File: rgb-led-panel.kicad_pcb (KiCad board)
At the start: 2 copper layers, 26 parts

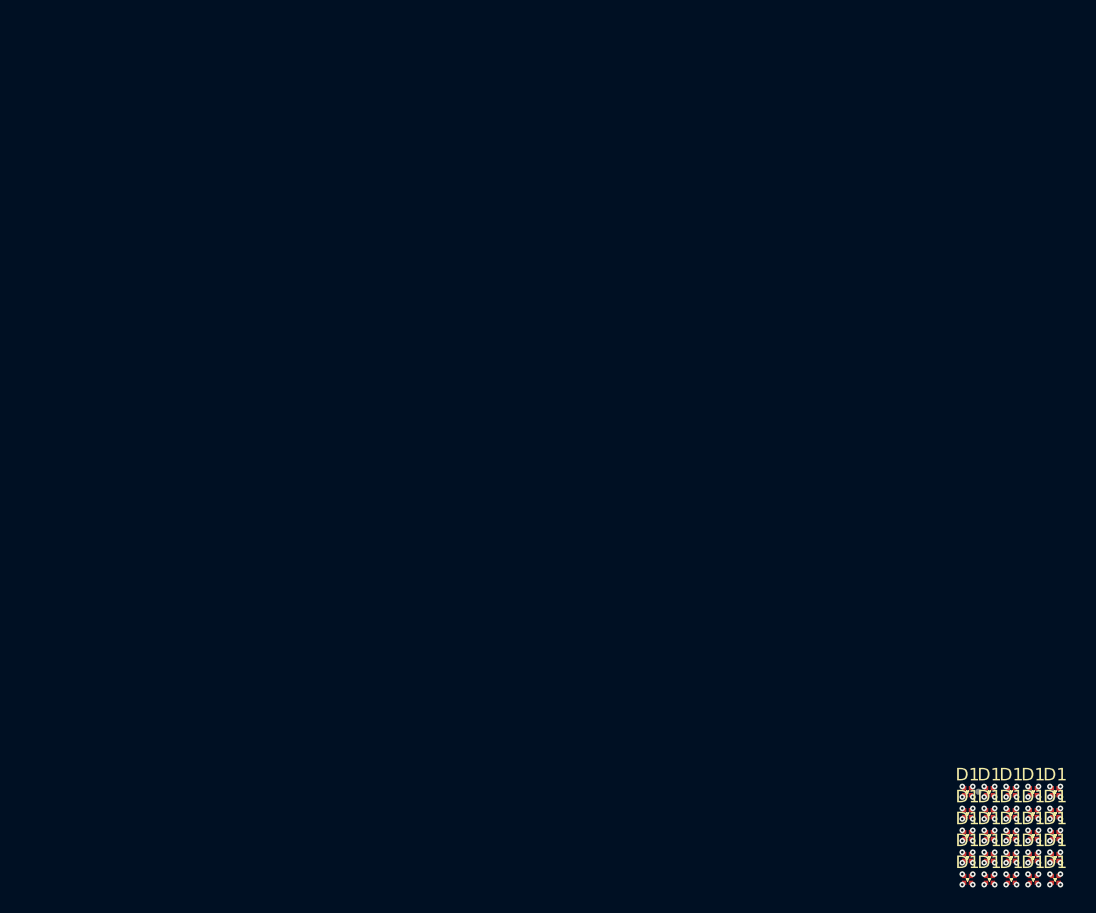
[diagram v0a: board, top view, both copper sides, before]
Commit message: Layout 16x16 RGB panel
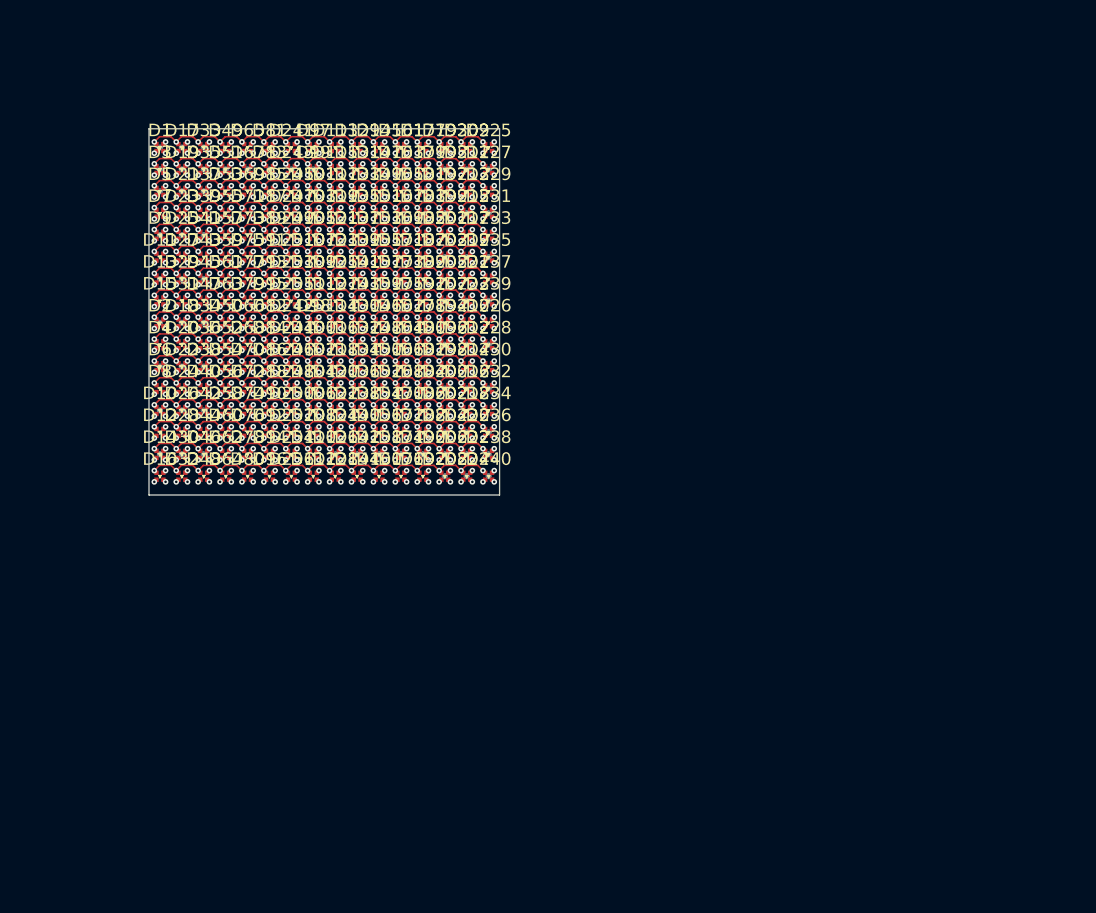
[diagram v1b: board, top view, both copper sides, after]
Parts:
- removed the D1 at (121.5, 108.5)
- removed the D1 at (114.5, 106.7)
- removed the D1 at (121.5, 105.0)
- removed the D1 at (119.8, 105.0)
- removed the D1 at (118.0, 105.0)
- removed the D1 at (116.2, 105.0)
- removed the D1 at (114.5, 105.0)
- removed the D1 at (121.5, 103.2)
- removed the D1 at (119.8, 103.2)
- removed the D1 at (118.0, 103.2)
- removed the D1 at (116.2, 103.2)
- removed the D1 at (119.8, 108.5)
- removed the D1 at (114.5, 103.2)
- removed the D1 at (121.5, 101.5)
- removed the D1 at (119.8, 101.5)
- removed the D1 at (118.0, 101.5)
- removed the D1 at (116.2, 101.5)
- removed the D1 at (114.5, 101.5)
- removed the D1 at (118.0, 108.5)
- removed the D1 at (116.2, 108.5)
- removed the D1 at (114.5, 108.5)
- removed the D1 at (121.5, 106.7)
- removed the D1 at (119.8, 106.7)
- removed the D1 at (118.0, 106.7)
- removed the D1 at (116.2, 106.7)
- removed REF**: TestPoint_0.5mm, TestPoint_Small:TestPoint_0.5mm
- added D1: LED_ARGB, LED_SMD_RGB:MHPA0808RGBDT, F.Cu at (50.0, 50.0)
- added D10: LED_ARGB, LED_SMD_RGB:MHPA0808RGBDT, F.Cu at (50.0, 71.0)
- added D100: LED_ARGB, LED_SMD_RGB:MHPA0808RGBDT, F.Cu at (62.2, 65.8)
- added D101: LED_ARGB, LED_SMD_RGB:MHPA0808RGBDT, F.Cu at (62.2, 53.5)
- added D102: LED_ARGB, LED_SMD_RGB:MHPA0808RGBDT, F.Cu at (62.2, 67.5)
- added D103: LED_ARGB, LED_SMD_RGB:MHPA0808RGBDT, F.Cu at (62.2, 55.2)
- added D104: LED_ARGB, LED_SMD_RGB:MHPA0808RGBDT, F.Cu at (62.2, 69.2)
- added D105: LED_ARGB, LED_SMD_RGB:MHPA0808RGBDT, F.Cu at (62.2, 57.0)
- added D106: LED_ARGB, LED_SMD_RGB:MHPA0808RGBDT, F.Cu at (62.2, 71.0)
- added D107: LED_ARGB, LED_SMD_RGB:MHPA0808RGBDT, F.Cu at (62.2, 58.8)
- added D108: LED_ARGB, LED_SMD_RGB:MHPA0808RGBDT, F.Cu at (62.2, 72.8)
- added D109: LED_ARGB, LED_SMD_RGB:MHPA0808RGBDT, F.Cu at (62.2, 60.5)
- added D11: LED_ARGB, LED_SMD_RGB:MHPA0808RGBDT, F.Cu at (50.0, 58.8)
- added D110: LED_ARGB, LED_SMD_RGB:MHPA0808RGBDT, F.Cu at (62.2, 74.5)
- added D111: LED_ARGB, LED_SMD_RGB:MHPA0808RGBDT, F.Cu at (62.2, 62.2)
- added D112: LED_ARGB, LED_SMD_RGB:MHPA0808RGBDT, F.Cu at (62.2, 76.2)
- added D113: LED_ARGB, LED_SMD_RGB:MHPA0808RGBDT, F.Cu at (64.0, 50.0)
- added D114: LED_ARGB, LED_SMD_RGB:MHPA0808RGBDT, F.Cu at (64.0, 64.0)
- added D115: LED_ARGB, LED_SMD_RGB:MHPA0808RGBDT, F.Cu at (64.0, 51.8)
- added D116: LED_ARGB, LED_SMD_RGB:MHPA0808RGBDT, F.Cu at (64.0, 65.8)
- added D117: LED_ARGB, LED_SMD_RGB:MHPA0808RGBDT, F.Cu at (64.0, 53.5)
- added D118: LED_ARGB, LED_SMD_RGB:MHPA0808RGBDT, F.Cu at (64.0, 67.5)
- added D119: LED_ARGB, LED_SMD_RGB:MHPA0808RGBDT, F.Cu at (64.0, 55.2)
- added D12: LED_ARGB, LED_SMD_RGB:MHPA0808RGBDT, F.Cu at (50.0, 72.8)
- added D120: LED_ARGB, LED_SMD_RGB:MHPA0808RGBDT, F.Cu at (64.0, 69.2)
- added D121: LED_ARGB, LED_SMD_RGB:MHPA0808RGBDT, F.Cu at (64.0, 57.0)
- added D122: LED_ARGB, LED_SMD_RGB:MHPA0808RGBDT, F.Cu at (64.0, 71.0)
- added D123: LED_ARGB, LED_SMD_RGB:MHPA0808RGBDT, F.Cu at (64.0, 58.8)
- added D124: LED_ARGB, LED_SMD_RGB:MHPA0808RGBDT, F.Cu at (64.0, 72.8)
- added D125: LED_ARGB, LED_SMD_RGB:MHPA0808RGBDT, F.Cu at (64.0, 60.5)
- added D126: LED_ARGB, LED_SMD_RGB:MHPA0808RGBDT, F.Cu at (64.0, 74.5)
- added D127: LED_ARGB, LED_SMD_RGB:MHPA0808RGBDT, F.Cu at (64.0, 62.2)
- added D128: LED_ARGB, LED_SMD_RGB:MHPA0808RGBDT, F.Cu at (64.0, 76.2)
- added D129: LED_ARGB, LED_SMD_RGB:MHPA0808RGBDT, F.Cu at (65.8, 50.0)
- added D13: LED_ARGB, LED_SMD_RGB:MHPA0808RGBDT, F.Cu at (50.0, 60.5)
- added D130: LED_ARGB, LED_SMD_RGB:MHPA0808RGBDT, F.Cu at (65.8, 64.0)
- added D131: LED_ARGB, LED_SMD_RGB:MHPA0808RGBDT, F.Cu at (65.8, 51.8)
- added D132: LED_ARGB, LED_SMD_RGB:MHPA0808RGBDT, F.Cu at (65.8, 65.8)
- added D133: LED_ARGB, LED_SMD_RGB:MHPA0808RGBDT, F.Cu at (65.8, 53.5)
- added D134: LED_ARGB, LED_SMD_RGB:MHPA0808RGBDT, F.Cu at (65.8, 67.5)
- added D135: LED_ARGB, LED_SMD_RGB:MHPA0808RGBDT, F.Cu at (65.8, 55.2)
- added D136: LED_ARGB, LED_SMD_RGB:MHPA0808RGBDT, F.Cu at (65.8, 69.2)
- added D137: LED_ARGB, LED_SMD_RGB:MHPA0808RGBDT, F.Cu at (65.8, 57.0)
- added D138: LED_ARGB, LED_SMD_RGB:MHPA0808RGBDT, F.Cu at (65.8, 71.0)
- added D139: LED_ARGB, LED_SMD_RGB:MHPA0808RGBDT, F.Cu at (65.8, 58.8)
- added D14: LED_ARGB, LED_SMD_RGB:MHPA0808RGBDT, F.Cu at (50.0, 74.5)
- added D140: LED_ARGB, LED_SMD_RGB:MHPA0808RGBDT, F.Cu at (65.8, 72.8)
- added D141: LED_ARGB, LED_SMD_RGB:MHPA0808RGBDT, F.Cu at (65.8, 60.5)
- added D142: LED_ARGB, LED_SMD_RGB:MHPA0808RGBDT, F.Cu at (65.8, 74.5)
- added D143: LED_ARGB, LED_SMD_RGB:MHPA0808RGBDT, F.Cu at (65.8, 62.2)
- added D144: LED_ARGB, LED_SMD_RGB:MHPA0808RGBDT, F.Cu at (65.8, 76.2)
- added D145: LED_ARGB, LED_SMD_RGB:MHPA0808RGBDT, F.Cu at (67.5, 50.0)
- added D146: LED_ARGB, LED_SMD_RGB:MHPA0808RGBDT, F.Cu at (67.5, 64.0)
- added D147: LED_ARGB, LED_SMD_RGB:MHPA0808RGBDT, F.Cu at (67.5, 51.8)
- added D148: LED_ARGB, LED_SMD_RGB:MHPA0808RGBDT, F.Cu at (67.5, 65.8)
- added D149: LED_ARGB, LED_SMD_RGB:MHPA0808RGBDT, F.Cu at (67.5, 53.5)
- added D15: LED_ARGB, LED_SMD_RGB:MHPA0808RGBDT, F.Cu at (50.0, 62.2)
- added D150: LED_ARGB, LED_SMD_RGB:MHPA0808RGBDT, F.Cu at (67.5, 67.5)
- added D151: LED_ARGB, LED_SMD_RGB:MHPA0808RGBDT, F.Cu at (67.5, 55.2)
- added D152: LED_ARGB, LED_SMD_RGB:MHPA0808RGBDT, F.Cu at (67.5, 69.2)
- added D153: LED_ARGB, LED_SMD_RGB:MHPA0808RGBDT, F.Cu at (67.5, 57.0)
- added D154: LED_ARGB, LED_SMD_RGB:MHPA0808RGBDT, F.Cu at (67.5, 71.0)
- added D155: LED_ARGB, LED_SMD_RGB:MHPA0808RGBDT, F.Cu at (67.5, 58.8)
- added D156: LED_ARGB, LED_SMD_RGB:MHPA0808RGBDT, F.Cu at (67.5, 72.8)
- added D157: LED_ARGB, LED_SMD_RGB:MHPA0808RGBDT, F.Cu at (67.5, 60.5)
- added D158: LED_ARGB, LED_SMD_RGB:MHPA0808RGBDT, F.Cu at (67.5, 74.5)
- added D159: LED_ARGB, LED_SMD_RGB:MHPA0808RGBDT, F.Cu at (67.5, 62.2)
- added D16: LED_ARGB, LED_SMD_RGB:MHPA0808RGBDT, F.Cu at (50.0, 76.2)
- added D160: LED_ARGB, LED_SMD_RGB:MHPA0808RGBDT, F.Cu at (67.5, 76.2)
- added D161: LED_ARGB, LED_SMD_RGB:MHPA0808RGBDT, F.Cu at (69.2, 50.0)
- added D162: LED_ARGB, LED_SMD_RGB:MHPA0808RGBDT, F.Cu at (69.2, 64.0)
- added D163: LED_ARGB, LED_SMD_RGB:MHPA0808RGBDT, F.Cu at (69.2, 51.8)
- added D164: LED_ARGB, LED_SMD_RGB:MHPA0808RGBDT, F.Cu at (69.2, 65.8)
- added D165: LED_ARGB, LED_SMD_RGB:MHPA0808RGBDT, F.Cu at (69.2, 53.5)
- added D166: LED_ARGB, LED_SMD_RGB:MHPA0808RGBDT, F.Cu at (69.2, 67.5)
- added D167: LED_ARGB, LED_SMD_RGB:MHPA0808RGBDT, F.Cu at (69.2, 55.2)
- added D168: LED_ARGB, LED_SMD_RGB:MHPA0808RGBDT, F.Cu at (69.2, 69.2)
- added D169: LED_ARGB, LED_SMD_RGB:MHPA0808RGBDT, F.Cu at (69.2, 57.0)
- added D17: LED_ARGB, LED_SMD_RGB:MHPA0808RGBDT, F.Cu at (51.8, 50.0)
- added D170: LED_ARGB, LED_SMD_RGB:MHPA0808RGBDT, F.Cu at (69.2, 71.0)
- added D171: LED_ARGB, LED_SMD_RGB:MHPA0808RGBDT, F.Cu at (69.2, 58.8)
- added D172: LED_ARGB, LED_SMD_RGB:MHPA0808RGBDT, F.Cu at (69.2, 72.8)
- added D173: LED_ARGB, LED_SMD_RGB:MHPA0808RGBDT, F.Cu at (69.2, 60.5)
- added D174: LED_ARGB, LED_SMD_RGB:MHPA0808RGBDT, F.Cu at (69.2, 74.5)
- added D175: LED_ARGB, LED_SMD_RGB:MHPA0808RGBDT, F.Cu at (69.2, 62.2)
- added D176: LED_ARGB, LED_SMD_RGB:MHPA0808RGBDT, F.Cu at (69.2, 76.2)
- added D177: LED_ARGB, LED_SMD_RGB:MHPA0808RGBDT, F.Cu at (71.0, 50.0)
- added D178: LED_ARGB, LED_SMD_RGB:MHPA0808RGBDT, F.Cu at (71.0, 64.0)
- added D179: LED_ARGB, LED_SMD_RGB:MHPA0808RGBDT, F.Cu at (71.0, 51.8)
- added D18: LED_ARGB, LED_SMD_RGB:MHPA0808RGBDT, F.Cu at (51.8, 64.0)
- added D180: LED_ARGB, LED_SMD_RGB:MHPA0808RGBDT, F.Cu at (71.0, 65.8)
- added D181: LED_ARGB, LED_SMD_RGB:MHPA0808RGBDT, F.Cu at (71.0, 53.5)
- added D182: LED_ARGB, LED_SMD_RGB:MHPA0808RGBDT, F.Cu at (71.0, 67.5)
- added D183: LED_ARGB, LED_SMD_RGB:MHPA0808RGBDT, F.Cu at (71.0, 55.2)
- added D184: LED_ARGB, LED_SMD_RGB:MHPA0808RGBDT, F.Cu at (71.0, 69.2)
- added D185: LED_ARGB, LED_SMD_RGB:MHPA0808RGBDT, F.Cu at (71.0, 57.0)
- added D186: LED_ARGB, LED_SMD_RGB:MHPA0808RGBDT, F.Cu at (71.0, 71.0)
- added D187: LED_ARGB, LED_SMD_RGB:MHPA0808RGBDT, F.Cu at (71.0, 58.8)
- added D188: LED_ARGB, LED_SMD_RGB:MHPA0808RGBDT, F.Cu at (71.0, 72.8)
- added D189: LED_ARGB, LED_SMD_RGB:MHPA0808RGBDT, F.Cu at (71.0, 60.5)
- added D19: LED_ARGB, LED_SMD_RGB:MHPA0808RGBDT, F.Cu at (51.8, 51.8)
- added D190: LED_ARGB, LED_SMD_RGB:MHPA0808RGBDT, F.Cu at (71.0, 74.5)
- added D191: LED_ARGB, LED_SMD_RGB:MHPA0808RGBDT, F.Cu at (71.0, 62.2)
- added D192: LED_ARGB, LED_SMD_RGB:MHPA0808RGBDT, F.Cu at (71.0, 76.2)
- added D193: LED_ARGB, LED_SMD_RGB:MHPA0808RGBDT, F.Cu at (72.8, 50.0)
- added D194: LED_ARGB, LED_SMD_RGB:MHPA0808RGBDT, F.Cu at (72.8, 64.0)
- added D195: LED_ARGB, LED_SMD_RGB:MHPA0808RGBDT, F.Cu at (72.8, 51.8)
- added D196: LED_ARGB, LED_SMD_RGB:MHPA0808RGBDT, F.Cu at (72.8, 65.8)
- added D197: LED_ARGB, LED_SMD_RGB:MHPA0808RGBDT, F.Cu at (72.8, 53.5)
- added D198: LED_ARGB, LED_SMD_RGB:MHPA0808RGBDT, F.Cu at (72.8, 67.5)
- added D199: LED_ARGB, LED_SMD_RGB:MHPA0808RGBDT, F.Cu at (72.8, 55.2)
- added D2: LED_ARGB, LED_SMD_RGB:MHPA0808RGBDT, F.Cu at (50.0, 64.0)
- added D20: LED_ARGB, LED_SMD_RGB:MHPA0808RGBDT, F.Cu at (51.8, 65.8)
- added D200: LED_ARGB, LED_SMD_RGB:MHPA0808RGBDT, F.Cu at (72.8, 69.2)
- added D201: LED_ARGB, LED_SMD_RGB:MHPA0808RGBDT, F.Cu at (72.8, 57.0)
- added D202: LED_ARGB, LED_SMD_RGB:MHPA0808RGBDT, F.Cu at (72.8, 71.0)
- added D203: LED_ARGB, LED_SMD_RGB:MHPA0808RGBDT, F.Cu at (72.8, 58.8)
- added D204: LED_ARGB, LED_SMD_RGB:MHPA0808RGBDT, F.Cu at (72.8, 72.8)
- added D205: LED_ARGB, LED_SMD_RGB:MHPA0808RGBDT, F.Cu at (72.8, 60.5)
- added D206: LED_ARGB, LED_SMD_RGB:MHPA0808RGBDT, F.Cu at (72.8, 74.5)
- added D207: LED_ARGB, LED_SMD_RGB:MHPA0808RGBDT, F.Cu at (72.8, 62.2)
- added D208: LED_ARGB, LED_SMD_RGB:MHPA0808RGBDT, F.Cu at (72.8, 76.2)
- added D209: LED_ARGB, LED_SMD_RGB:MHPA0808RGBDT, F.Cu at (74.5, 50.0)
- added D21: LED_ARGB, LED_SMD_RGB:MHPA0808RGBDT, F.Cu at (51.8, 53.5)
- added D210: LED_ARGB, LED_SMD_RGB:MHPA0808RGBDT, F.Cu at (74.5, 64.0)
- added D211: LED_ARGB, LED_SMD_RGB:MHPA0808RGBDT, F.Cu at (74.5, 51.8)
- added D212: LED_ARGB, LED_SMD_RGB:MHPA0808RGBDT, F.Cu at (74.5, 65.8)
- added D213: LED_ARGB, LED_SMD_RGB:MHPA0808RGBDT, F.Cu at (74.5, 53.5)
- added D214: LED_ARGB, LED_SMD_RGB:MHPA0808RGBDT, F.Cu at (74.5, 67.5)
- added D215: LED_ARGB, LED_SMD_RGB:MHPA0808RGBDT, F.Cu at (74.5, 55.2)
- added D216: LED_ARGB, LED_SMD_RGB:MHPA0808RGBDT, F.Cu at (74.5, 69.2)
- added D217: LED_ARGB, LED_SMD_RGB:MHPA0808RGBDT, F.Cu at (74.5, 57.0)
- added D218: LED_ARGB, LED_SMD_RGB:MHPA0808RGBDT, F.Cu at (74.5, 71.0)
- added D219: LED_ARGB, LED_SMD_RGB:MHPA0808RGBDT, F.Cu at (74.5, 58.8)
- added D22: LED_ARGB, LED_SMD_RGB:MHPA0808RGBDT, F.Cu at (51.8, 67.5)
- added D220: LED_ARGB, LED_SMD_RGB:MHPA0808RGBDT, F.Cu at (74.5, 72.8)
- added D221: LED_ARGB, LED_SMD_RGB:MHPA0808RGBDT, F.Cu at (74.5, 60.5)
- added D222: LED_ARGB, LED_SMD_RGB:MHPA0808RGBDT, F.Cu at (74.5, 74.5)
- added D223: LED_ARGB, LED_SMD_RGB:MHPA0808RGBDT, F.Cu at (74.5, 62.2)
- added D224: LED_ARGB, LED_SMD_RGB:MHPA0808RGBDT, F.Cu at (74.5, 76.2)
- added D225: LED_ARGB, LED_SMD_RGB:MHPA0808RGBDT, F.Cu at (76.2, 50.0)
- added D226: LED_ARGB, LED_SMD_RGB:MHPA0808RGBDT, F.Cu at (76.2, 64.0)
- added D227: LED_ARGB, LED_SMD_RGB:MHPA0808RGBDT, F.Cu at (76.2, 51.8)
- added D228: LED_ARGB, LED_SMD_RGB:MHPA0808RGBDT, F.Cu at (76.2, 65.8)
- added D229: LED_ARGB, LED_SMD_RGB:MHPA0808RGBDT, F.Cu at (76.2, 53.5)
- added D23: LED_ARGB, LED_SMD_RGB:MHPA0808RGBDT, F.Cu at (51.8, 55.2)
- added D230: LED_ARGB, LED_SMD_RGB:MHPA0808RGBDT, F.Cu at (76.2, 67.5)
- added D231: LED_ARGB, LED_SMD_RGB:MHPA0808RGBDT, F.Cu at (76.2, 55.2)
- added D232: LED_ARGB, LED_SMD_RGB:MHPA0808RGBDT, F.Cu at (76.2, 69.2)
- added D233: LED_ARGB, LED_SMD_RGB:MHPA0808RGBDT, F.Cu at (76.2, 57.0)
- added D234: LED_ARGB, LED_SMD_RGB:MHPA0808RGBDT, F.Cu at (76.2, 71.0)
- added D235: LED_ARGB, LED_SMD_RGB:MHPA0808RGBDT, F.Cu at (76.2, 58.8)
- added D236: LED_ARGB, LED_SMD_RGB:MHPA0808RGBDT, F.Cu at (76.2, 72.8)
- added D237: LED_ARGB, LED_SMD_RGB:MHPA0808RGBDT, F.Cu at (76.2, 60.5)
- added D238: LED_ARGB, LED_SMD_RGB:MHPA0808RGBDT, F.Cu at (76.2, 74.5)
- added D239: LED_ARGB, LED_SMD_RGB:MHPA0808RGBDT, F.Cu at (76.2, 62.2)
- added D24: LED_ARGB, LED_SMD_RGB:MHPA0808RGBDT, F.Cu at (51.8, 69.2)
- added D240: LED_ARGB, LED_SMD_RGB:MHPA0808RGBDT, F.Cu at (76.2, 76.2)
- added D241: LED_ARGB, LED_SMD_RGB:MHPA0808RGBDT, F.Cu at (60.5, 50.0)
- added D242: LED_ARGB, LED_SMD_RGB:MHPA0808RGBDT, F.Cu at (60.5, 64.0)
- added D243: LED_ARGB, LED_SMD_RGB:MHPA0808RGBDT, F.Cu at (60.5, 51.8)
- added D244: LED_ARGB, LED_SMD_RGB:MHPA0808RGBDT, F.Cu at (60.5, 65.8)
- added D245: LED_ARGB, LED_SMD_RGB:MHPA0808RGBDT, F.Cu at (60.5, 53.5)
- added D246: LED_ARGB, LED_SMD_RGB:MHPA0808RGBDT, F.Cu at (60.5, 67.5)
- added D247: LED_ARGB, LED_SMD_RGB:MHPA0808RGBDT, F.Cu at (60.5, 55.2)
- added D248: LED_ARGB, LED_SMD_RGB:MHPA0808RGBDT, F.Cu at (60.5, 69.2)
- added D249: LED_ARGB, LED_SMD_RGB:MHPA0808RGBDT, F.Cu at (60.5, 57.0)
- added D25: LED_ARGB, LED_SMD_RGB:MHPA0808RGBDT, F.Cu at (51.8, 57.0)
- added D250: LED_ARGB, LED_SMD_RGB:MHPA0808RGBDT, F.Cu at (60.5, 71.0)
- added D251: LED_ARGB, LED_SMD_RGB:MHPA0808RGBDT, F.Cu at (60.5, 58.8)
- added D252: LED_ARGB, LED_SMD_RGB:MHPA0808RGBDT, F.Cu at (60.5, 72.8)
- added D253: LED_ARGB, LED_SMD_RGB:MHPA0808RGBDT, F.Cu at (60.5, 60.5)
- added D254: LED_ARGB, LED_SMD_RGB:MHPA0808RGBDT, F.Cu at (60.5, 74.5)
- added D255: LED_ARGB, LED_SMD_RGB:MHPA0808RGBDT, F.Cu at (60.5, 62.2)
- added D256: LED_ARGB, LED_SMD_RGB:MHPA0808RGBDT, F.Cu at (60.5, 76.2)
- added D26: LED_ARGB, LED_SMD_RGB:MHPA0808RGBDT, F.Cu at (51.8, 71.0)
- added D27: LED_ARGB, LED_SMD_RGB:MHPA0808RGBDT, F.Cu at (51.8, 58.8)
- added D28: LED_ARGB, LED_SMD_RGB:MHPA0808RGBDT, F.Cu at (51.8, 72.8)
- added D29: LED_ARGB, LED_SMD_RGB:MHPA0808RGBDT, F.Cu at (51.8, 60.5)
- added D3: LED_ARGB, LED_SMD_RGB:MHPA0808RGBDT, F.Cu at (50.0, 51.8)
- added D30: LED_ARGB, LED_SMD_RGB:MHPA0808RGBDT, F.Cu at (51.8, 74.5)
- added D31: LED_ARGB, LED_SMD_RGB:MHPA0808RGBDT, F.Cu at (51.8, 62.2)
- added D32: LED_ARGB, LED_SMD_RGB:MHPA0808RGBDT, F.Cu at (51.8, 76.2)
- added D33: LED_ARGB, LED_SMD_RGB:MHPA0808RGBDT, F.Cu at (53.5, 50.0)
- added D34: LED_ARGB, LED_SMD_RGB:MHPA0808RGBDT, F.Cu at (53.5, 64.0)
- added D35: LED_ARGB, LED_SMD_RGB:MHPA0808RGBDT, F.Cu at (53.5, 51.8)
- added D36: LED_ARGB, LED_SMD_RGB:MHPA0808RGBDT, F.Cu at (53.5, 65.8)
- added D37: LED_ARGB, LED_SMD_RGB:MHPA0808RGBDT, F.Cu at (53.5, 53.5)
- added D38: LED_ARGB, LED_SMD_RGB:MHPA0808RGBDT, F.Cu at (53.5, 67.5)
- added D39: LED_ARGB, LED_SMD_RGB:MHPA0808RGBDT, F.Cu at (53.5, 55.2)
- added D4: LED_ARGB, LED_SMD_RGB:MHPA0808RGBDT, F.Cu at (50.0, 65.8)
- added D40: LED_ARGB, LED_SMD_RGB:MHPA0808RGBDT, F.Cu at (53.5, 69.2)
- added D41: LED_ARGB, LED_SMD_RGB:MHPA0808RGBDT, F.Cu at (53.5, 57.0)
- added D42: LED_ARGB, LED_SMD_RGB:MHPA0808RGBDT, F.Cu at (53.5, 71.0)
- added D43: LED_ARGB, LED_SMD_RGB:MHPA0808RGBDT, F.Cu at (53.5, 58.8)
- added D44: LED_ARGB, LED_SMD_RGB:MHPA0808RGBDT, F.Cu at (53.5, 72.8)
- added D45: LED_ARGB, LED_SMD_RGB:MHPA0808RGBDT, F.Cu at (53.5, 60.5)
- added D46: LED_ARGB, LED_SMD_RGB:MHPA0808RGBDT, F.Cu at (53.5, 74.5)
- added D47: LED_ARGB, LED_SMD_RGB:MHPA0808RGBDT, F.Cu at (53.5, 62.2)
- added D48: LED_ARGB, LED_SMD_RGB:MHPA0808RGBDT, F.Cu at (53.5, 76.2)
- added D49: LED_ARGB, LED_SMD_RGB:MHPA0808RGBDT, F.Cu at (55.2, 50.0)
- added D5: LED_ARGB, LED_SMD_RGB:MHPA0808RGBDT, F.Cu at (50.0, 53.5)
- added D50: LED_ARGB, LED_SMD_RGB:MHPA0808RGBDT, F.Cu at (55.2, 64.0)
- added D51: LED_ARGB, LED_SMD_RGB:MHPA0808RGBDT, F.Cu at (55.2, 51.8)
- added D52: LED_ARGB, LED_SMD_RGB:MHPA0808RGBDT, F.Cu at (55.2, 65.8)
- added D53: LED_ARGB, LED_SMD_RGB:MHPA0808RGBDT, F.Cu at (55.2, 53.5)
- added D54: LED_ARGB, LED_SMD_RGB:MHPA0808RGBDT, F.Cu at (55.2, 67.5)
- added D55: LED_ARGB, LED_SMD_RGB:MHPA0808RGBDT, F.Cu at (55.2, 55.2)
- added D56: LED_ARGB, LED_SMD_RGB:MHPA0808RGBDT, F.Cu at (55.2, 69.2)
- added D57: LED_ARGB, LED_SMD_RGB:MHPA0808RGBDT, F.Cu at (55.2, 57.0)
- added D58: LED_ARGB, LED_SMD_RGB:MHPA0808RGBDT, F.Cu at (55.2, 71.0)
- added D59: LED_ARGB, LED_SMD_RGB:MHPA0808RGBDT, F.Cu at (55.2, 58.8)
- added D6: LED_ARGB, LED_SMD_RGB:MHPA0808RGBDT, F.Cu at (50.0, 67.5)
- added D60: LED_ARGB, LED_SMD_RGB:MHPA0808RGBDT, F.Cu at (55.2, 72.8)
- added D61: LED_ARGB, LED_SMD_RGB:MHPA0808RGBDT, F.Cu at (55.2, 60.5)
- added D62: LED_ARGB, LED_SMD_RGB:MHPA0808RGBDT, F.Cu at (55.2, 74.5)
- added D63: LED_ARGB, LED_SMD_RGB:MHPA0808RGBDT, F.Cu at (55.2, 62.2)
- added D64: LED_ARGB, LED_SMD_RGB:MHPA0808RGBDT, F.Cu at (55.2, 76.2)
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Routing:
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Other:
- board outline added: 28 x 29.2 mm
- copper layers 2 -> 4

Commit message: DFM
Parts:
- added H1: ToolingHole, ToolingHole:ToolingHole_JLCSMT, F.Cu at (75.1, 82.0)
- added H2: ToolingHole, ToolingHole:ToolingHole_JLCSMT, F.Cu at (51.1, 44.2)
- added REF**: Perforation_0.4mm, Perforation:Perforation_0.4mm, F.Cu at (75.1, 77.8)
- added REF**: Perforation_0.4mm, Perforation:Perforation_0.4mm, F.Cu at (52.6, 77.8)
- added REF**: Perforation_0.4mm, Perforation:Perforation_0.4mm, F.Cu at (75.1, 48.5)
- added REF**: Perforation_0.4mm, Perforation:Perforation_0.4mm, F.Cu at (73.6, 48.5)
- added REF**: Perforation_0.4mm, Perforation:Perforation_0.4mm, F.Cu at (74.4, 48.5)
- added REF**: Perforation_0.4mm, Perforation:Perforation_0.4mm, F.Cu at (75.9, 48.5)
- added REF**: Perforation_0.4mm, Perforation:Perforation_0.4mm, F.Cu at (76.6, 48.5)
- added REF**: Perforation_0.4mm, Perforation:Perforation_0.4mm, F.Cu at (52.6, 48.5)
- added REF**: Perforation_0.4mm, Perforation:Perforation_0.4mm, F.Cu at (51.9, 48.5)
- added REF**: Perforation_0.4mm, Perforation:Perforation_0.4mm, F.Cu at (51.1, 48.5)
- added REF**: Perforation_0.4mm, Perforation:Perforation_0.4mm, F.Cu at (50.4, 48.5)
- added REF**: Perforation_0.4mm, Perforation:Perforation_0.4mm, F.Cu at (73.6, 77.8)
- added REF**: Perforation_0.4mm, Perforation:Perforation_0.4mm, F.Cu at (49.6, 48.5)
- added REF**: Perforation_0.4mm, Perforation:Perforation_0.4mm, F.Cu at (74.4, 77.8)
- added REF**: Perforation_0.4mm, Perforation:Perforation_0.4mm, F.Cu at (75.9, 77.8)
- added REF**: Perforation_0.4mm, Perforation:Perforation_0.4mm, F.Cu at (76.6, 77.8)
- added REF**: Perforation_0.4mm, Perforation:Perforation_0.4mm, F.Cu at (51.1, 77.8)
- added REF**: Perforation_0.4mm, Perforation:Perforation_0.4mm, F.Cu at (49.6, 77.8)
- added REF**: Perforation_0.4mm, Perforation:Perforation_0.4mm, F.Cu at (50.4, 77.8)
- added REF**: Perforation_0.4mm, Perforation:Perforation_0.4mm, F.Cu at (51.9, 77.8)
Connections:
- D100 pad 2: /Leds/C1/R10 -> /Leds/C8/R10
- D100 pad 3: /Leds/C1/G10 -> /Leds/C8/G10
- D100 pad 4: /Leds/C1/B10 -> /Leds/C8/B10
- D101 pad 2: /Leds/C1/R3 -> /Leds/C8/R3
- D101 pad 3: /Leds/C1/G3 -> /Leds/C8/G3
- D101 pad 4: /Leds/C1/B3 -> /Leds/C8/B3
- D102 pad 2: /Leds/C1/R11 -> /Leds/C8/R11
- D102 pad 3: /Leds/C1/G11 -> /Leds/C8/G11
- D102 pad 4: /Leds/C1/B11 -> /Leds/C8/B11
- D103 pad 2: /Leds/C1/R4 -> /Leds/C8/R4
- D103 pad 3: /Leds/C1/G4 -> /Leds/C8/G4
- D103 pad 4: /Leds/C1/B4 -> /Leds/C8/B4
- D104 pad 2: /Leds/C1/R12 -> /Leds/C8/R12
- D104 pad 3: /Leds/C1/G12 -> /Leds/C8/G12
- D104 pad 4: /Leds/C1/B12 -> /Leds/C8/B12
- D105 pad 2: /Leds/C1/R5 -> /Leds/C8/R5
- D105 pad 3: /Leds/C1/G5 -> /Leds/C8/G5
- D105 pad 4: /Leds/C1/B5 -> /Leds/C8/B5
- D106 pad 2: /Leds/C1/R13 -> /Leds/C8/R13
- D106 pad 3: /Leds/C1/G13 -> /Leds/C8/G13
- D106 pad 4: /Leds/C1/B13 -> /Leds/C8/B13
- D107 pad 2: /Leds/C1/R6 -> /Leds/C8/R6
- D107 pad 3: /Leds/C1/G6 -> /Leds/C8/G6
- D107 pad 4: /Leds/C1/B6 -> /Leds/C8/B6
- D108 pad 2: /Leds/C1/R14 -> /Leds/C8/R14
- D108 pad 3: /Leds/C1/G14 -> /Leds/C8/G14
- D108 pad 4: /Leds/C1/B14 -> /Leds/C8/B14
- D109 pad 2: /Leds/C1/R7 -> /Leds/C8/R7
- D109 pad 3: /Leds/C1/G7 -> /Leds/C8/G7
- D109 pad 4: /Leds/C1/B7 -> /Leds/C8/B7
- D110 pad 2: /Leds/C1/R15 -> /Leds/C8/R15
- D110 pad 3: /Leds/C1/G15 -> /Leds/C8/G15
- D110 pad 4: /Leds/C1/B15 -> /Leds/C8/B15
- D111 pad 2: /Leds/C1/R8 -> /Leds/C8/R8
- D111 pad 3: /Leds/C1/G8 -> /Leds/C8/G8
- D111 pad 4: /Leds/C1/B8 -> /Leds/C8/B8
- D112 pad 2: /Leds/C1/R16 -> /Leds/C8/R16
- D112 pad 3: /Leds/C1/G16 -> /Leds/C8/G16
- D112 pad 4: /Leds/C1/B16 -> /Leds/C8/B16
- D113 pad 2: /Leds/C1/R1 -> /Leds/C9/R1
- D113 pad 3: /Leds/C1/G1 -> /Leds/C9/G1
- D113 pad 4: /Leds/C1/B1 -> /Leds/C9/B1
- D114 pad 2: /Leds/C1/R9 -> /Leds/C9/R9
- D114 pad 3: /Leds/C1/G9 -> /Leds/C9/G9
- D114 pad 4: /Leds/C1/B9 -> /Leds/C9/B9
- D115 pad 2: /Leds/C1/R2 -> /Leds/C9/R2
- D115 pad 3: /Leds/C1/G2 -> /Leds/C9/G2
- D115 pad 4: /Leds/C1/B2 -> /Leds/C9/B2
- D116 pad 2: /Leds/C1/R10 -> /Leds/C9/R10
- D116 pad 3: /Leds/C1/G10 -> /Leds/C9/G10
- D116 pad 4: /Leds/C1/B10 -> /Leds/C9/B10
- D117 pad 2: /Leds/C1/R3 -> /Leds/C9/R3
- D117 pad 3: /Leds/C1/G3 -> /Leds/C9/G3
- D117 pad 4: /Leds/C1/B3 -> /Leds/C9/B3
- D118 pad 2: /Leds/C1/R11 -> /Leds/C9/R11
- D118 pad 3: /Leds/C1/G11 -> /Leds/C9/G11
- D118 pad 4: /Leds/C1/B11 -> /Leds/C9/B11
- D119 pad 2: /Leds/C1/R4 -> /Leds/C9/R4
- D119 pad 3: /Leds/C1/G4 -> /Leds/C9/G4
- D119 pad 4: /Leds/C1/B4 -> /Leds/C9/B4
- D120 pad 2: /Leds/C1/R12 -> /Leds/C9/R12
- D120 pad 3: /Leds/C1/G12 -> /Leds/C9/G12
- D120 pad 4: /Leds/C1/B12 -> /Leds/C9/B12
- D121 pad 2: /Leds/C1/R5 -> /Leds/C9/R5
- D121 pad 3: /Leds/C1/G5 -> /Leds/C9/G5
- D121 pad 4: /Leds/C1/B5 -> /Leds/C9/B5
- D122 pad 2: /Leds/C1/R13 -> /Leds/C9/R13
- D122 pad 3: /Leds/C1/G13 -> /Leds/C9/G13
- D122 pad 4: /Leds/C1/B13 -> /Leds/C9/B13
- D123 pad 2: /Leds/C1/R6 -> /Leds/C9/R6
- D123 pad 3: /Leds/C1/G6 -> /Leds/C9/G6
- D123 pad 4: /Leds/C1/B6 -> /Leds/C9/B6
- D124 pad 2: /Leds/C1/R14 -> /Leds/C9/R14
- D124 pad 3: /Leds/C1/G14 -> /Leds/C9/G14
- D124 pad 4: /Leds/C1/B14 -> /Leds/C9/B14
- D125 pad 2: /Leds/C1/R7 -> /Leds/C9/R7
- D125 pad 3: /Leds/C1/G7 -> /Leds/C9/G7
- D125 pad 4: /Leds/C1/B7 -> /Leds/C9/B7
- D126 pad 2: /Leds/C1/R15 -> /Leds/C9/R15
- D126 pad 3: /Leds/C1/G15 -> /Leds/C9/G15
- D126 pad 4: /Leds/C1/B15 -> /Leds/C9/B15
- D127 pad 2: /Leds/C1/R8 -> /Leds/C9/R8
- D127 pad 3: /Leds/C1/G8 -> /Leds/C9/G8
- D127 pad 4: /Leds/C1/B8 -> /Leds/C9/B8
- D128 pad 2: /Leds/C1/R16 -> /Leds/C9/R16
- D128 pad 3: /Leds/C1/G16 -> /Leds/C9/G16
- D128 pad 4: /Leds/C1/B16 -> /Leds/C9/B16
- D129 pad 2: /Leds/C1/R1 -> /Leds/C10/R1
- D129 pad 3: /Leds/C1/G1 -> /Leds/C10/G1
- D129 pad 4: /Leds/C1/B1 -> /Leds/C10/B1
- D130 pad 2: /Leds/C1/R9 -> /Leds/C10/R9
- D130 pad 3: /Leds/C1/G9 -> /Leds/C10/G9
- D130 pad 4: /Leds/C1/B9 -> /Leds/C10/B9
- D131 pad 2: /Leds/C1/R2 -> /Leds/C10/R2
- D131 pad 3: /Leds/C1/G2 -> /Leds/C10/G2
- D131 pad 4: /Leds/C1/B2 -> /Leds/C10/B2
- D132 pad 2: /Leds/C1/R10 -> /Leds/C10/R10
- D132 pad 3: /Leds/C1/G10 -> /Leds/C10/G10
- D132 pad 4: /Leds/C1/B10 -> /Leds/C10/B10
- D133 pad 2: /Leds/C1/R3 -> /Leds/C10/R3
- D133 pad 3: /Leds/C1/G3 -> /Leds/C10/G3
- D133 pad 4: /Leds/C1/B3 -> /Leds/C10/B3
- D134 pad 2: /Leds/C1/R11 -> /Leds/C10/R11
- D134 pad 3: /Leds/C1/G11 -> /Leds/C10/G11
- D134 pad 4: /Leds/C1/B11 -> /Leds/C10/B11
- D135 pad 2: /Leds/C1/R4 -> /Leds/C10/R4
- D135 pad 3: /Leds/C1/G4 -> /Leds/C10/G4
- D135 pad 4: /Leds/C1/B4 -> /Leds/C10/B4
- D136 pad 2: /Leds/C1/R12 -> /Leds/C10/R12
- D136 pad 3: /Leds/C1/G12 -> /Leds/C10/G12
- D136 pad 4: /Leds/C1/B12 -> /Leds/C10/B12
- D137 pad 2: /Leds/C1/R5 -> /Leds/C10/R5
- D137 pad 3: /Leds/C1/G5 -> /Leds/C10/G5
- D137 pad 4: /Leds/C1/B5 -> /Leds/C10/B5
- D138 pad 2: /Leds/C1/R13 -> /Leds/C10/R13
- D138 pad 3: /Leds/C1/G13 -> /Leds/C10/G13
- D138 pad 4: /Leds/C1/B13 -> /Leds/C10/B13
- D139 pad 2: /Leds/C1/R6 -> /Leds/C10/R6
- D139 pad 3: /Leds/C1/G6 -> /Leds/C10/G6
- D139 pad 4: /Leds/C1/B6 -> /Leds/C10/B6
- D140 pad 2: /Leds/C1/R14 -> /Leds/C10/R14
- D140 pad 3: /Leds/C1/G14 -> /Leds/C10/G14
- D140 pad 4: /Leds/C1/B14 -> /Leds/C10/B14
- D141 pad 2: /Leds/C1/R7 -> /Leds/C10/R7
- D141 pad 3: /Leds/C1/G7 -> /Leds/C10/G7
- D141 pad 4: /Leds/C1/B7 -> /Leds/C10/B7
- D142 pad 2: /Leds/C1/R15 -> /Leds/C10/R15
- D142 pad 3: /Leds/C1/G15 -> /Leds/C10/G15
- D142 pad 4: /Leds/C1/B15 -> /Leds/C10/B15
- D143 pad 2: /Leds/C1/R8 -> /Leds/C10/R8
- D143 pad 3: /Leds/C1/G8 -> /Leds/C10/G8
- D143 pad 4: /Leds/C1/B8 -> /Leds/C10/B8
- D144 pad 2: /Leds/C1/R16 -> /Leds/C10/R16
- D144 pad 3: /Leds/C1/G16 -> /Leds/C10/G16
- D144 pad 4: /Leds/C1/B16 -> /Leds/C10/B16
- D145 pad 2: /Leds/C1/R1 -> /Leds/C11/R1
- D145 pad 3: /Leds/C1/G1 -> /Leds/C11/G1
- D145 pad 4: /Leds/C1/B1 -> /Leds/C11/B1
- D146 pad 2: /Leds/C1/R9 -> /Leds/C11/R9
- D146 pad 3: /Leds/C1/G9 -> /Leds/C11/G9
- D146 pad 4: /Leds/C1/B9 -> /Leds/C11/B9
- D147 pad 2: /Leds/C1/R2 -> /Leds/C11/R2
- D147 pad 3: /Leds/C1/G2 -> /Leds/C11/G2
- D147 pad 4: /Leds/C1/B2 -> /Leds/C11/B2
- D148 pad 2: /Leds/C1/R10 -> /Leds/C11/R10
- D148 pad 3: /Leds/C1/G10 -> /Leds/C11/G10
- D148 pad 4: /Leds/C1/B10 -> /Leds/C11/B10
- D149 pad 2: /Leds/C1/R3 -> /Leds/C11/R3
- D149 pad 3: /Leds/C1/G3 -> /Leds/C11/G3
- D149 pad 4: /Leds/C1/B3 -> /Leds/C11/B3
- D150 pad 2: /Leds/C1/R11 -> /Leds/C11/R11
- D150 pad 3: /Leds/C1/G11 -> /Leds/C11/G11
- D150 pad 4: /Leds/C1/B11 -> /Leds/C11/B11
- D151 pad 2: /Leds/C1/R4 -> /Leds/C11/R4
- D151 pad 3: /Leds/C1/G4 -> /Leds/C11/G4
- D151 pad 4: /Leds/C1/B4 -> /Leds/C11/B4
- D152 pad 2: /Leds/C1/R12 -> /Leds/C11/R12
- D152 pad 3: /Leds/C1/G12 -> /Leds/C11/G12
- D152 pad 4: /Leds/C1/B12 -> /Leds/C11/B12
- D153 pad 2: /Leds/C1/R5 -> /Leds/C11/R5
- D153 pad 3: /Leds/C1/G5 -> /Leds/C11/G5
- D153 pad 4: /Leds/C1/B5 -> /Leds/C11/B5
- D154 pad 2: /Leds/C1/R13 -> /Leds/C11/R13
- D154 pad 3: /Leds/C1/G13 -> /Leds/C11/G13
- D154 pad 4: /Leds/C1/B13 -> /Leds/C11/B13
- D155 pad 2: /Leds/C1/R6 -> /Leds/C11/R6
- D155 pad 3: /Leds/C1/G6 -> /Leds/C11/G6
- D155 pad 4: /Leds/C1/B6 -> /Leds/C11/B6
- D156 pad 2: /Leds/C1/R14 -> /Leds/C11/R14
- D156 pad 3: /Leds/C1/G14 -> /Leds/C11/G14
- D156 pad 4: /Leds/C1/B14 -> /Leds/C11/B14
- D157 pad 2: /Leds/C1/R7 -> /Leds/C11/R7
- D157 pad 3: /Leds/C1/G7 -> /Leds/C11/G7
- D157 pad 4: /Leds/C1/B7 -> /Leds/C11/B7
- D158 pad 2: /Leds/C1/R15 -> /Leds/C11/R15
- D158 pad 3: /Leds/C1/G15 -> /Leds/C11/G15
- D158 pad 4: /Leds/C1/B15 -> /Leds/C11/B15
- D159 pad 2: /Leds/C1/R8 -> /Leds/C11/R8
- D159 pad 3: /Leds/C1/G8 -> /Leds/C11/G8
- D159 pad 4: /Leds/C1/B8 -> /Leds/C11/B8
- D160 pad 2: /Leds/C1/R16 -> /Leds/C11/R16
- D160 pad 3: /Leds/C1/G16 -> /Leds/C11/G16
- D160 pad 4: /Leds/C1/B16 -> /Leds/C11/B16
- D161 pad 2: /Leds/C1/R1 -> /Leds/C12/R1
- D161 pad 3: /Leds/C1/G1 -> /Leds/C12/G1
- D161 pad 4: /Leds/C1/B1 -> /Leds/C12/B1
- D162 pad 2: /Leds/C1/R9 -> /Leds/C12/R9
- D162 pad 3: /Leds/C1/G9 -> /Leds/C12/G9
- D162 pad 4: /Leds/C1/B9 -> /Leds/C12/B9
- D163 pad 2: /Leds/C1/R2 -> /Leds/C12/R2
- D163 pad 3: /Leds/C1/G2 -> /Leds/C12/G2
- D163 pad 4: /Leds/C1/B2 -> /Leds/C12/B2
- D164 pad 2: /Leds/C1/R10 -> /Leds/C12/R10
- D164 pad 3: /Leds/C1/G10 -> /Leds/C12/G10
- D164 pad 4: /Leds/C1/B10 -> /Leds/C12/B10
- D165 pad 2: /Leds/C1/R3 -> /Leds/C12/R3
- D165 pad 3: /Leds/C1/G3 -> /Leds/C12/G3
- D165 pad 4: /Leds/C1/B3 -> /Leds/C12/B3
- D166 pad 2: /Leds/C1/R11 -> /Leds/C12/R11
- D166 pad 3: /Leds/C1/G11 -> /Leds/C12/G11
- D166 pad 4: /Leds/C1/B11 -> /Leds/C12/B11
- D167 pad 2: /Leds/C1/R4 -> /Leds/C12/R4
- D167 pad 3: /Leds/C1/G4 -> /Leds/C12/G4
- D167 pad 4: /Leds/C1/B4 -> /Leds/C12/B4
- D168 pad 2: /Leds/C1/R12 -> /Leds/C12/R12
- D168 pad 3: /Leds/C1/G12 -> /Leds/C12/G12
- D168 pad 4: /Leds/C1/B12 -> /Leds/C12/B12
- D169 pad 2: /Leds/C1/R5 -> /Leds/C12/R5
- D169 pad 3: /Leds/C1/G5 -> /Leds/C12/G5
- D169 pad 4: /Leds/C1/B5 -> /Leds/C12/B5
- D17 pad 2: /Leds/C1/R1 -> /Leds/C2/R1
- D17 pad 3: /Leds/C1/G1 -> /Leds/C2/G1
- D17 pad 4: /Leds/C1/B1 -> /Leds/C2/B1
- D170 pad 2: /Leds/C1/R13 -> /Leds/C12/R13
- D170 pad 3: /Leds/C1/G13 -> /Leds/C12/G13
- D170 pad 4: /Leds/C1/B13 -> /Leds/C12/B13
- D171 pad 2: /Leds/C1/R6 -> /Leds/C12/R6
- D171 pad 3: /Leds/C1/G6 -> /Leds/C12/G6
- D171 pad 4: /Leds/C1/B6 -> /Leds/C12/B6
- D172 pad 2: /Leds/C1/R14 -> /Leds/C12/R14
- D172 pad 3: /Leds/C1/G14 -> /Leds/C12/G14
- D172 pad 4: /Leds/C1/B14 -> /Leds/C12/B14
- D173 pad 2: /Leds/C1/R7 -> /Leds/C12/R7
- D173 pad 3: /Leds/C1/G7 -> /Leds/C12/G7
- D173 pad 4: /Leds/C1/B7 -> /Leds/C12/B7
- D174 pad 2: /Leds/C1/R15 -> /Leds/C12/R15
- D174 pad 3: /Leds/C1/G15 -> /Leds/C12/G15
- D174 pad 4: /Leds/C1/B15 -> /Leds/C12/B15
- D175 pad 2: /Leds/C1/R8 -> /Leds/C12/R8
- D175 pad 3: /Leds/C1/G8 -> /Leds/C12/G8
- D175 pad 4: /Leds/C1/B8 -> /Leds/C12/B8
- D176 pad 2: /Leds/C1/R16 -> /Leds/C12/R16
- D176 pad 3: /Leds/C1/G16 -> /Leds/C12/G16
- D176 pad 4: /Leds/C1/B16 -> /Leds/C12/B16
- D177 pad 2: /Leds/C1/R1 -> /Leds/C13/R1
- D177 pad 3: /Leds/C1/G1 -> /Leds/C13/G1
- D177 pad 4: /Leds/C1/B1 -> /Leds/C13/B1
- D178 pad 2: /Leds/C1/R9 -> /Leds/C13/R9
- D178 pad 3: /Leds/C1/G9 -> /Leds/C13/G9
- D178 pad 4: /Leds/C1/B9 -> /Leds/C13/B9
- D179 pad 2: /Leds/C1/R2 -> /Leds/C13/R2
- D179 pad 3: /Leds/C1/G2 -> /Leds/C13/G2
- D179 pad 4: /Leds/C1/B2 -> /Leds/C13/B2
- D18 pad 2: /Leds/C1/R9 -> /Leds/C2/R9
- D18 pad 3: /Leds/C1/G9 -> /Leds/C2/G9
- D18 pad 4: /Leds/C1/B9 -> /Leds/C2/B9
- D180 pad 2: /Leds/C1/R10 -> /Leds/C13/R10
- D180 pad 3: /Leds/C1/G10 -> /Leds/C13/G10
- D180 pad 4: /Leds/C1/B10 -> /Leds/C13/B10
- D181 pad 2: /Leds/C1/R3 -> /Leds/C13/R3
- D181 pad 3: /Leds/C1/G3 -> /Leds/C13/G3
- D181 pad 4: /Leds/C1/B3 -> /Leds/C13/B3
- D182 pad 2: /Leds/C1/R11 -> /Leds/C13/R11
- D182 pad 3: /Leds/C1/G11 -> /Leds/C13/G11
- D182 pad 4: /Leds/C1/B11 -> /Leds/C13/B11
- D183 pad 2: /Leds/C1/R4 -> /Leds/C13/R4
- D183 pad 3: /Leds/C1/G4 -> /Leds/C13/G4
- D183 pad 4: /Leds/C1/B4 -> /Leds/C13/B4
- D184 pad 2: /Leds/C1/R12 -> /Leds/C13/R12
- D184 pad 3: /Leds/C1/G12 -> /Leds/C13/G12
- D184 pad 4: /Leds/C1/B12 -> /Leds/C13/B12
- D185 pad 2: /Leds/C1/R5 -> /Leds/C13/R5
- D185 pad 3: /Leds/C1/G5 -> /Leds/C13/G5
- D185 pad 4: /Leds/C1/B5 -> /Leds/C13/B5
- D186 pad 2: /Leds/C1/R13 -> /Leds/C13/R13
- D186 pad 3: /Leds/C1/G13 -> /Leds/C13/G13
- D186 pad 4: /Leds/C1/B13 -> /Leds/C13/B13
- D187 pad 2: /Leds/C1/R6 -> /Leds/C13/R6
- D187 pad 3: /Leds/C1/G6 -> /Leds/C13/G6
- D187 pad 4: /Leds/C1/B6 -> /Leds/C13/B6
- D188 pad 2: /Leds/C1/R14 -> /Leds/C13/R14
- D188 pad 3: /Leds/C1/G14 -> /Leds/C13/G14
- D188 pad 4: /Leds/C1/B14 -> /Leds/C13/B14
- D189 pad 2: /Leds/C1/R7 -> /Leds/C13/R7
- D189 pad 3: /Leds/C1/G7 -> /Leds/C13/G7
- D189 pad 4: /Leds/C1/B7 -> /Leds/C13/B7
- D19 pad 2: /Leds/C1/R2 -> /Leds/C2/R2
- D19 pad 3: /Leds/C1/G2 -> /Leds/C2/G2
- D19 pad 4: /Leds/C1/B2 -> /Leds/C2/B2
- D190 pad 2: /Leds/C1/R15 -> /Leds/C13/R15
- D190 pad 3: /Leds/C1/G15 -> /Leds/C13/G15
- D190 pad 4: /Leds/C1/B15 -> /Leds/C13/B15
- D191 pad 2: /Leds/C1/R8 -> /Leds/C13/R8
- D191 pad 3: /Leds/C1/G8 -> /Leds/C13/G8
- D191 pad 4: /Leds/C1/B8 -> /Leds/C13/B8
- D192 pad 2: /Leds/C1/R16 -> /Leds/C13/R16
- D192 pad 3: /Leds/C1/G16 -> /Leds/C13/G16
- D192 pad 4: /Leds/C1/B16 -> /Leds/C13/B16
- D193 pad 2: /Leds/C1/R1 -> /Leds/C14/R1
- D193 pad 3: /Leds/C1/G1 -> /Leds/C14/G1
- D193 pad 4: /Leds/C1/B1 -> /Leds/C14/B1
- D194 pad 2: /Leds/C1/R9 -> /Leds/C14/R9
- D194 pad 3: /Leds/C1/G9 -> /Leds/C14/G9
- D194 pad 4: /Leds/C1/B9 -> /Leds/C14/B9
- D195 pad 2: /Leds/C1/R2 -> /Leds/C14/R2
- D195 pad 3: /Leds/C1/G2 -> /Leds/C14/G2
- D195 pad 4: /Leds/C1/B2 -> /Leds/C14/B2
- D196 pad 2: /Leds/C1/R10 -> /Leds/C14/R10
- D196 pad 3: /Leds/C1/G10 -> /Leds/C14/G10
- D196 pad 4: /Leds/C1/B10 -> /Leds/C14/B10
- D197 pad 2: /Leds/C1/R3 -> /Leds/C14/R3
- D197 pad 3: /Leds/C1/G3 -> /Leds/C14/G3
- D197 pad 4: /Leds/C1/B3 -> /Leds/C14/B3
- D198 pad 2: /Leds/C1/R11 -> /Leds/C14/R11
- D198 pad 3: /Leds/C1/G11 -> /Leds/C14/G11
- D198 pad 4: /Leds/C1/B11 -> /Leds/C14/B11
- D199 pad 2: /Leds/C1/R4 -> /Leds/C14/R4
- D199 pad 3: /Leds/C1/G4 -> /Leds/C14/G4
- D199 pad 4: /Leds/C1/B4 -> /Leds/C14/B4
- D20 pad 2: /Leds/C1/R10 -> /Leds/C2/R10
- D20 pad 3: /Leds/C1/G10 -> /Leds/C2/G10
- D20 pad 4: /Leds/C1/B10 -> /Leds/C2/B10
- D200 pad 2: /Leds/C1/R12 -> /Leds/C14/R12
- D200 pad 3: /Leds/C1/G12 -> /Leds/C14/G12
- D200 pad 4: /Leds/C1/B12 -> /Leds/C14/B12
- D201 pad 2: /Leds/C1/R5 -> /Leds/C14/R5
- D201 pad 3: /Leds/C1/G5 -> /Leds/C14/G5
- D201 pad 4: /Leds/C1/B5 -> /Leds/C14/B5
- D202 pad 2: /Leds/C1/R13 -> /Leds/C14/R13
- D202 pad 3: /Leds/C1/G13 -> /Leds/C14/G13
- D202 pad 4: /Leds/C1/B13 -> /Leds/C14/B13
- D203 pad 2: /Leds/C1/R6 -> /Leds/C14/R6
- D203 pad 3: /Leds/C1/G6 -> /Leds/C14/G6
- D203 pad 4: /Leds/C1/B6 -> /Leds/C14/B6
- D204 pad 2: /Leds/C1/R14 -> /Leds/C14/R14
- D204 pad 3: /Leds/C1/G14 -> /Leds/C14/G14
- D204 pad 4: /Leds/C1/B14 -> /Leds/C14/B14
- D205 pad 2: /Leds/C1/R7 -> /Leds/C14/R7
- D205 pad 3: /Leds/C1/G7 -> /Leds/C14/G7
- D205 pad 4: /Leds/C1/B7 -> /Leds/C14/B7
- D206 pad 2: /Leds/C1/R15 -> /Leds/C14/R15
- D206 pad 3: /Leds/C1/G15 -> /Leds/C14/G15
- D206 pad 4: /Leds/C1/B15 -> /Leds/C14/B15
- D207 pad 2: /Leds/C1/R8 -> /Leds/C14/R8
- D207 pad 3: /Leds/C1/G8 -> /Leds/C14/G8
- D207 pad 4: /Leds/C1/B8 -> /Leds/C14/B8
- D208 pad 2: /Leds/C1/R16 -> /Leds/C14/R16
- D208 pad 3: /Leds/C1/G16 -> /Leds/C14/G16
- D208 pad 4: /Leds/C1/B16 -> /Leds/C14/B16
- D209 pad 2: /Leds/C1/R1 -> /Leds/C15/R1
- D209 pad 3: /Leds/C1/G1 -> /Leds/C15/G1
- D209 pad 4: /Leds/C1/B1 -> /Leds/C15/B1
- D21 pad 2: /Leds/C1/R3 -> /Leds/C2/R3
- D21 pad 3: /Leds/C1/G3 -> /Leds/C2/G3
- D21 pad 4: /Leds/C1/B3 -> /Leds/C2/B3
- D210 pad 2: /Leds/C1/R9 -> /Leds/C15/R9
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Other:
- board size 28 x 29.2 mm -> 28 x 40.8 mm

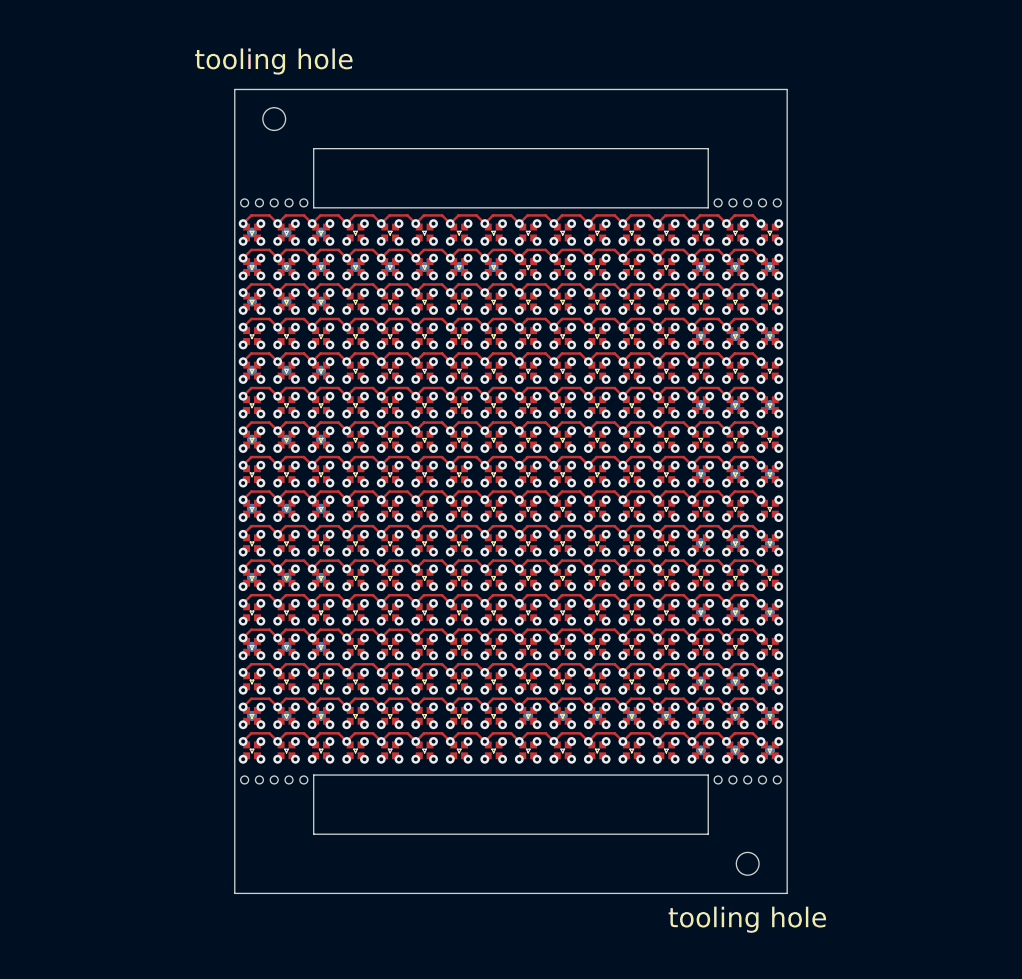
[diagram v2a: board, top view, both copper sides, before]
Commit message: Add rails to protect left and right pcb edges in manufacturing
Without the rails the left and right edges of the LED PCB can end up with
burrs from other PCBs in the same panel.
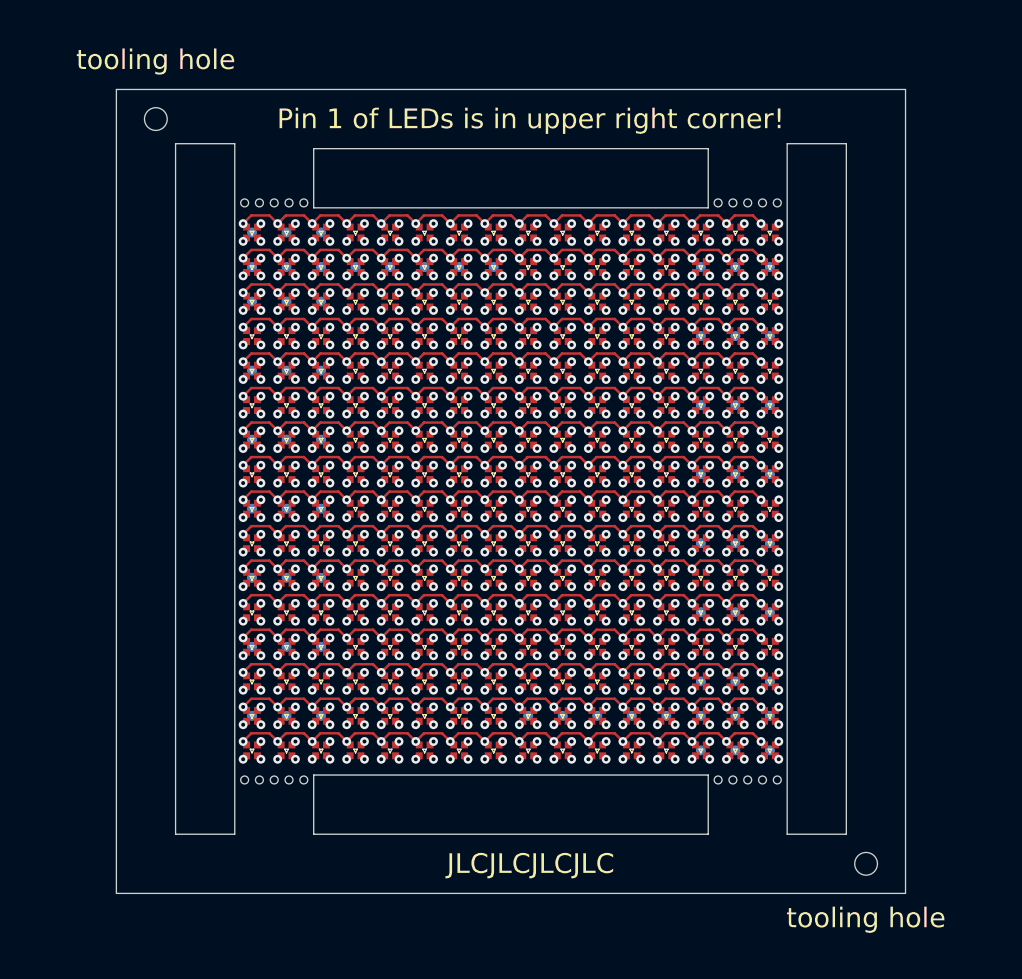
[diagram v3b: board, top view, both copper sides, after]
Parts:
- moved H1 6.00 mm to (81.1, 82.0)
- moved H2 6.00 mm to (45.1, 44.2)
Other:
- board size 28 x 40.8 mm -> 40 x 40.8 mm
- board text added: "JLCJLCJLCJLC"
- board text added: "Pin 1 of LEDs is in upper right corner!"
